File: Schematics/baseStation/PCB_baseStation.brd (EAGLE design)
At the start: 53 x 60 mm, 41 parts, among them U1 ATMEGA328P, U2 MCP1824ST-3302E/DB, Y2 16MHz

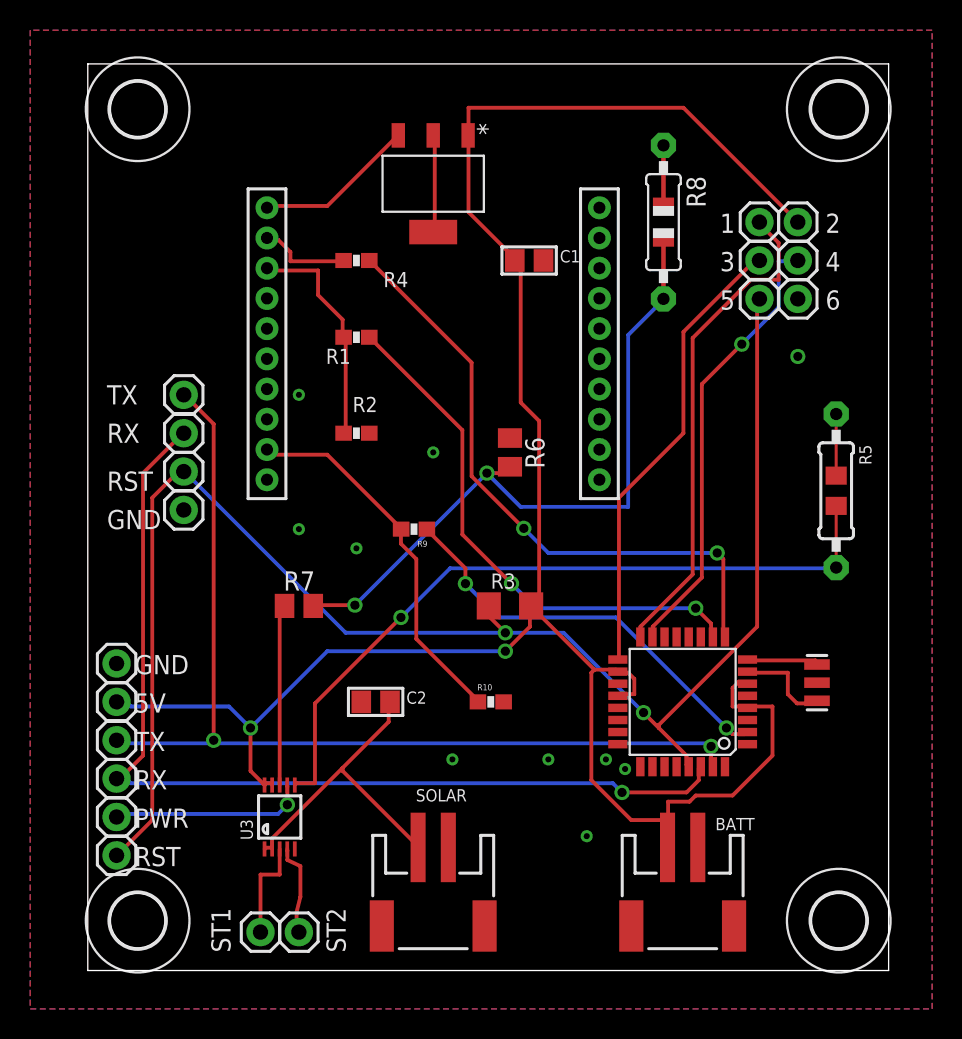
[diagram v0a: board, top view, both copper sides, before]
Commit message: Base Station PCB Improvements
Base_SP 1.2
moved components around to group them better
corrected xbee pin 9 to be connected from arduino PD4 to PD7
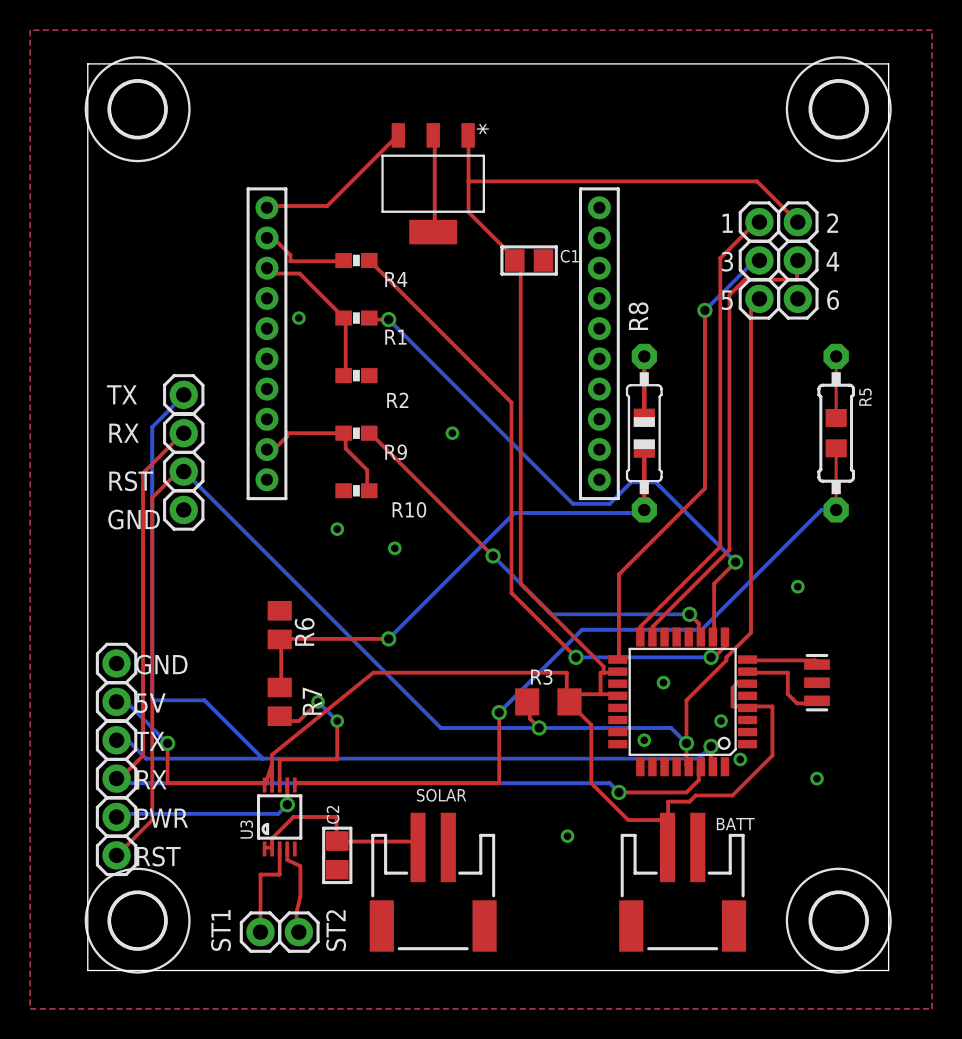
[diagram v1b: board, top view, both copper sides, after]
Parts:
- moved R6 19.1 mm to (12.7, 22.9)
- moved R10 16.6 mm to (17.8, 31.8), turned to 180 degrees
- moved R8 14.0 mm to (36.8, 35.6)
- moved C2 10.5 mm to (16.5, 7.62), turned to 90 degrees
- moved R9 7.41 mm to (17.8, 35.6)
- moved R3 6.84 mm to (30.5, 17.8)
- moved R7 6.48 mm to (12.7, 17.8), turned to 90 degrees
- moved R5 3.81 mm to (49.5, 35.6)
- moved R2 3.81 mm to (17.8, 39.4)
- moved R1 1.27 mm to (17.8, 43.2)
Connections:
- removed net PD4: R9.1, U1.2
- new net PD7: R9.1, U1.11
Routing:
- net PD7: track 0.00 -> 28.0 mm, vias 0 -> 2
- net PD4: track 27.5 -> 0.00 mm, vias 2 -> 0
- net N$6: track 24.7 -> 10.2 mm
- net N$13: track 42.1 -> 30.9 mm, vias 2 -> 1
- net N$9: track 20.8 -> 13.3 mm
- net N$19: track 64.8 -> 71.6 mm, vias 2 -> 1
- net N$3: track 15.1 -> 10.6 mm
- net DIN: track 35.5 -> 37.7 mm
- net 1: track 32.8 -> 30.9 mm
- net VCC: track 144.3 -> 142.6 mm, vias 2 -> 1
- net DOUT: track 41.2 -> 42.9 mm
- net 4: track 29.6 -> 30.9 mm, vias 1 -> 0
- net N$10: track 44.9 -> 46.1 mm
- net N$15: track 12.2 -> 13.2 mm, vias 0 -> 2
- net RST: track 102.7 -> 103.3 mm
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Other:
- board text added: "BASE_SP 1.2"
- board text removed: "BASE_SP 1.1"
